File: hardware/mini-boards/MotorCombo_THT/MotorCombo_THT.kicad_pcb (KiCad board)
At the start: 2 copper layers, 75 x 55 mm, 30 parts

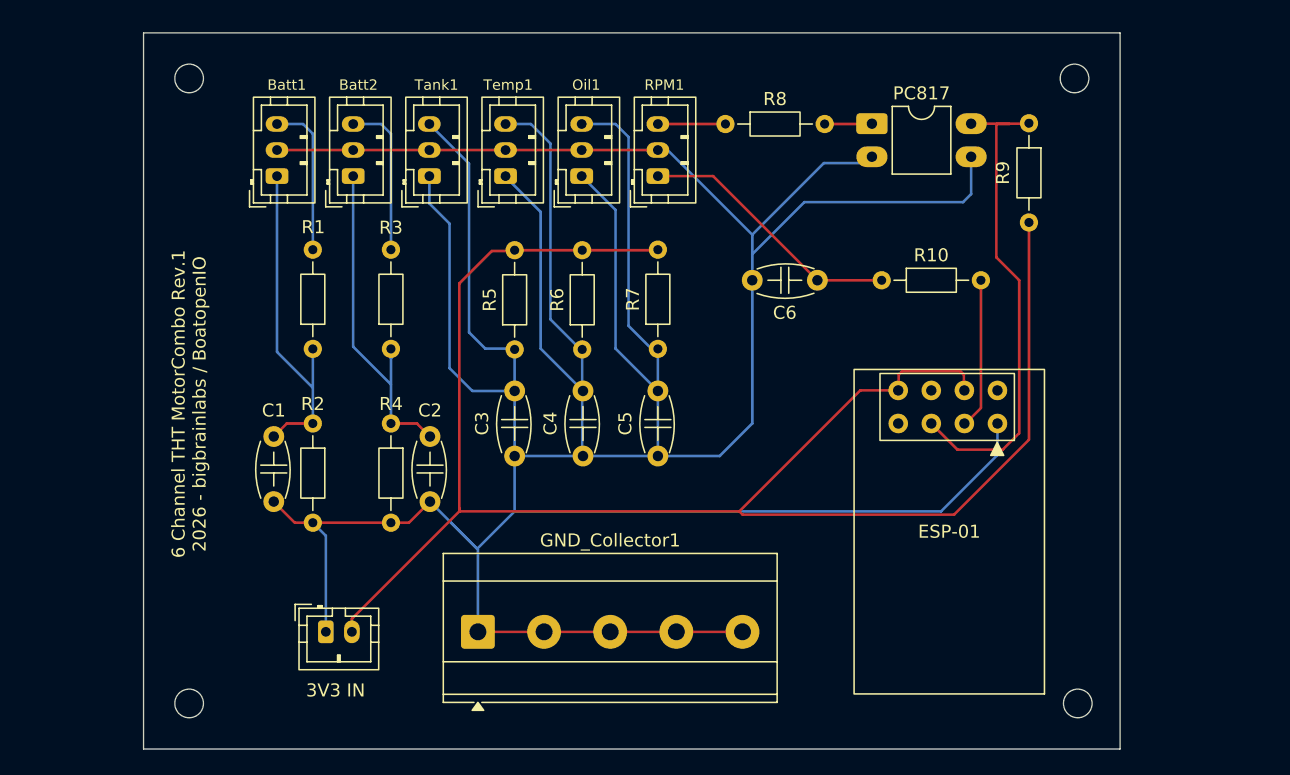
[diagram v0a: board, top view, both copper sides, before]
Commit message: MotorCombo THT: Jumper-Doku, Rev.1-Bild, ESP-01-Firmware; SMD-Variante entfernt
- README (DE/EN): neuer Abschnitt "Kanalmodus — Jumper (Kanäle 1–5)":
  JP1 (P1=3.3V/Pullup, P3=SIG-IN/Teiler, P2=gemeinsam), JP2 und R2 wählen
  Pull-up- vs. Spannungsteiler-Modus je Kanal. Hinweis unter der Kanaltabelle.
- Neues Platinenbild MotorCombo_THT.jpg (Rev.1-Render) eingebunden.
- esp_firmware/esp_firmware.ino wiederhergestellt (ESP-01 Drehzahl: GPIO0
  Impulszählung vom Optokoppler, GPIO2 PWM zum MUX).
- KiCad-Projekt aktualisiert; alte Gerber entfernt.
- MotorCombo/ (SMD-Variante) entfernt.

Co-Authored-By: Claude Opus 4.8 <noreply@anthropic.com>
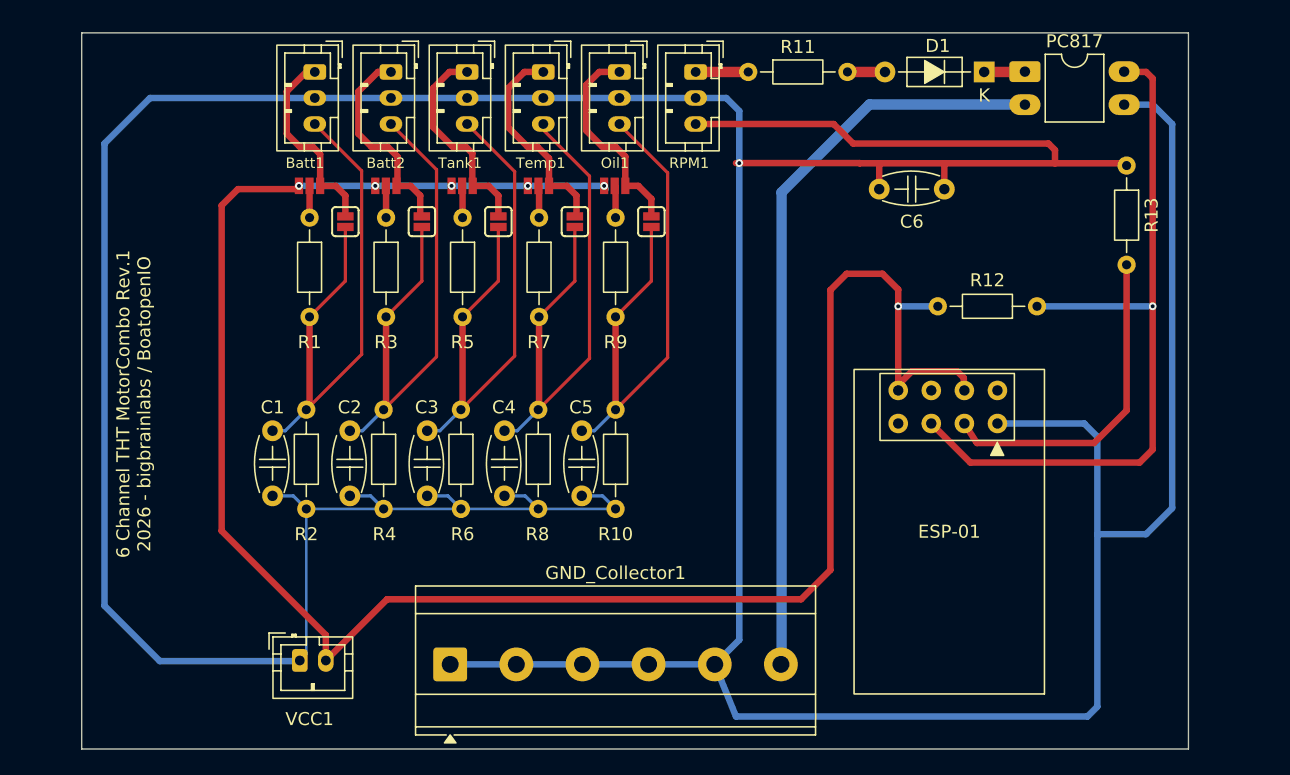
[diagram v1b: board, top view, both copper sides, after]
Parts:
- removed REF** (x4): MountingHole_2.2mm_M2, MountingHole:MountingHole_2.2mm_M2
- added D1: 1N4148, PCM_Diode_THT_AKL:D_DO-35_SOD27_P7.62mm_Horizontal, F.Cu at (118.6, 71.0)
- added JP1: Jumper_3_Open, PCM_SparkFun-Jumper:Jumper_3_NO_NoSilk, F.Cu at (66.8, 79.8)
- added JP10: Jumper_2_Open, PCM_SparkFun-Jumper:Jumper_2_NO, F.Cu at (93.0, 82.5)
- added JP2: Jumper_2_Open, PCM_SparkFun-Jumper:Jumper_2_NO, F.Cu at (69.5, 82.5)
- added JP3: Jumper_3_Open, PCM_SparkFun-Jumper:Jumper_3_NO_NoSilk, F.Cu at (72.6, 79.8)
- added JP4: Jumper_2_Open, PCM_SparkFun-Jumper:Jumper_2_NO, F.Cu at (75.4, 82.5)
- added JP5: Jumper_3_Open, PCM_SparkFun-Jumper:Jumper_3_NO_NoSilk, F.Cu at (78.5, 79.8)
- added JP6: Jumper_2_Open, PCM_SparkFun-Jumper:Jumper_2_NO, F.Cu at (81.2, 82.5)
- added JP7: Jumper_3_Open, PCM_SparkFun-Jumper:Jumper_3_NO_NoSilk, F.Cu at (84.3, 79.8)
- added JP8: Jumper_2_Open, PCM_SparkFun-Jumper:Jumper_2_NO, F.Cu at (87.1, 82.5)
- added JP9: Jumper_3_Open, PCM_SparkFun-Jumper:Jumper_3_NO_NoSilk, F.Cu at (90.2, 79.8)
- added R10: R, Resistor_THT:R_Axial_DIN0204_L3.6mm_D1.6mm_P7.62mm_Horizontal, F.Cu at (90.2, 96.9)
- added R8: R, Resistor_THT:R_Axial_DIN0204_L3.6mm_D1.6mm_P7.62mm_Horizontal, F.Cu at (84.3, 96.9)
- added R9: R, Resistor_THT:R_Axial_DIN0204_L3.6mm_D1.6mm_P7.62mm_Horizontal, F.Cu at (90.2, 82.2)
- GND_Collector1: footprint TerminalBlock_Phoenix:TerminalBlock_Phoenix_MKDS-3-5-5.08_1x05_P5.08mm_Horizontal -> TerminalBlock_Phoenix:TerminalBlock_Phoenix_MKDS-3-6-5.08_1x06_P5.08mm_Horizontal
- R11: renamed from R8; value R -> 1k
- R12: renamed from R9; value R -> 10k
- R13: renamed from R10; value R -> 10k
- VCC1: renamed from 3V3 IN
- moved R13 20.8 mm to (129.5, 78.2), turned to -90 degrees
- moved R12 14.1 mm to (122.6, 89.0), turned to 180 degrees
- moved R7 13.6 mm to (84.4, 82.2), turned to -90 degrees
- moved PC817 12.4 mm to (121.7, 71.0)
- moved R5 10.9 mm to (78.5, 82.2), turned to -90 degrees
- moved R6 10.4 mm to (78.4, 96.9), turned to -90 degrees
- moved R3 10.1 mm to (72.6, 82.2), turned to -90 degrees
- moved R1 10.1 mm to (66.8, 82.2), turned to -90 degrees
- moved Batt1 8.51 mm to (67.2, 71.0), turned to -90 degrees
- moved Batt2 8.51 mm to (73.0, 71.0), turned to -90 degrees
- moved RPM1 8.51 mm to (96.4, 71.0), turned to -90 degrees
- moved Temp1 8.51 mm to (84.7, 71.0), turned to -90 degrees
- moved Oil1 8.51 mm to (90.5, 71.0), turned to -90 degrees
- moved Tank1 8.51 mm to (78.8, 71.0), turned to -90 degrees
- moved C6 8.46 mm to (110.5, 80.0), turned to 0 degrees
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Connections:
- Batt1 pad 1: Net-(Batt1-Pad1) -> Net-(JP1-B)
- Batt2 pad 1: Net-(Batt2-Pad1) -> Net-(JP3-B)
- C3 pad 2: Net-(C3-Pad2) -> Net-(JP6-A)
- C4 pad 2: Net-(C4-Pad2) -> Net-(JP8-A)
- C5 pad 2: Net-(C5-Pad2) -> Net-(JP10-A)
- C6 pad 1: Net-(C6-Pad1) -> GND
- ESP-01 pad 2: Net-(ESP-01-GPIO2) -> Net-(ESP-01-GPIO0)
- ESP-01 pad 3: Net-(ESP-01-GPIO0) -> unconnected-(ESP-01-UTXD-Pad2)
- ESP-01 pad 4: unconnected-(ESP-01-URXD-Pad8) -> unconnected-(ESP-01-RST-Pad6)
- ESP-01 pad 5: unconnected-(ESP-01-RST-Pad5) -> Net-(ESP-01-GPIO2)
- ESP-01 pad 6: Net-(ESP-01-CH_PD) -> unconnected-(ESP-01-URXD-Pad7)
- ESP-01 pad 7: unconnected-(ESP-01-RST-Pad5) -> Net-(ESP-01-CH_PD)
- ESP-01 pad 8: unconnected-(ESP-01-URXD-Pad8) -> Net-(ESP-01-CH_PD)
- Oil1 pad 1: Net-(C5-Pad2) -> Net-(JP10-B)
- Oil1 pad 3: Net-(C5-Pad2) -> Net-(JP10-A)
- PC817 pad 1: Net-(PC817-Pad1) -> Net-(D1-K)
- PC817 pad 2: GND -> Net-(GND_Collector1-Pin_6)
- R1 pad 1: Net-(Batt1-Pad1) -> Net-(JP1-C)
- R11 pad 2: Net-(PC817-Pad1) -> Net-(D1-A)
- R13 pad 1: Net-(C6-Pad1) -> GND
- R3 pad 1: Net-(Batt2-Pad1) -> Net-(JP3-C)
- R5 pad 1: Net-(ESP-01-CH_PD) -> Net-(JP5-C)
- R5 pad 2: Net-(C3-Pad2) -> Net-(JP6-A)
- R6 pad 1: Net-(ESP-01-CH_PD) -> Net-(JP6-A)
- R6 pad 2: Net-(C4-Pad2) -> GND
- R7 pad 1: Net-(ESP-01-CH_PD) -> Net-(JP7-C)
- R7 pad 2: Net-(C5-Pad2) -> Net-(JP8-A)
- RPM1 pad 3: Net-(C6-Pad1) -> GND
- Tank1 pad 1: Net-(C3-Pad2) -> Net-(JP5-B)
- Tank1 pad 3: Net-(C3-Pad2) -> Net-(JP6-A)
- Temp1 pad 1: Net-(C4-Pad2) -> Net-(JP7-B)
- Temp1 pad 3: Net-(C4-Pad2) -> Net-(JP8-A)
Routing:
- net GND: track 171.5 -> 384.0 mm, vias 0 -> 1
- net Net-(C3-Pad2): track 89.9 -> 0.00 mm
- net Net-(ESP-01-CH_PD): track 74.0 -> 148.6 mm, vias 0 -> 6
- net Net-(GND_Collector1-Pin_6): track 0.00 -> 57.8 mm
- net Net-(JP6-A): track 0.00 -> 43.6 mm
- net Net-(JP10-A): track 0.00 -> 43.6 mm
- net Net-(JP8-A): track 0.00 -> 43.5 mm
- net unconnected-(ESP-01-UTXD-Pad1): track 41.3 -> 0.00 mm
- net Net-(C5-Pad2): track 40.3 -> 0.00 mm
- net Net-(C4-Pad2): track 40.0 -> 0.00 mm
- net unconnected-(ESP-01-URXD-Pad8): track 37.8 -> 0.00 mm
- net unconnected-(ESP-01-UTXD-Pad2): track 0.00 -> 25.8 mm
- net Net-(JP4-A): track 20.9 -> 43.6 mm
- net Net-(JP2-A): track 21.4 -> 43.7 mm
- net Net-(C6-Pad1): track 21.1 -> 0.00 mm
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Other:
- board size 75 x 55 mm -> 85 x 55 mm

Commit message: Hardware: Gerber & KiCad-Projektdateien aktualisiert
MotorCombo_THT und v2/input-board: Gerber, Bohrdateien, ZIP,
Bestueckungs-CSV und KiCad-Projektdateien neu erzeugt.

Co-Authored-By: Claude Opus 4.8 <noreply@anthropic.com>
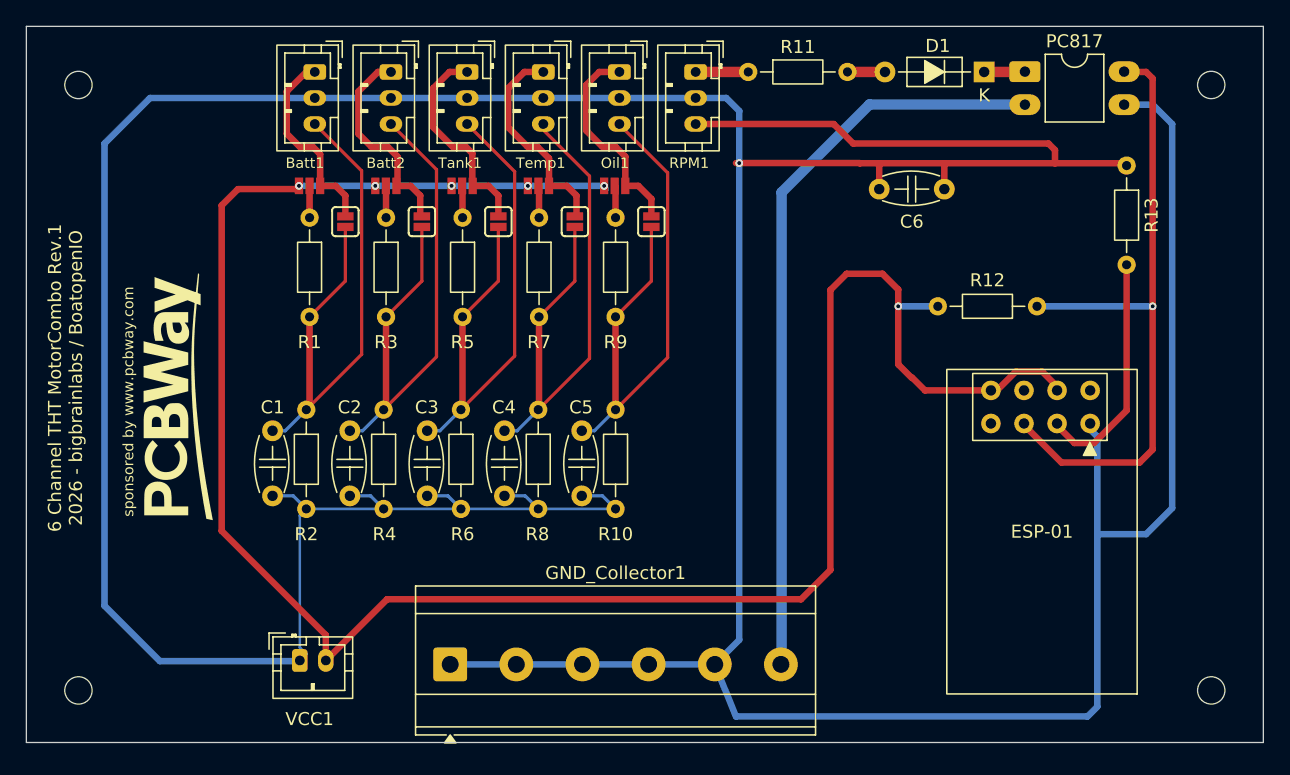
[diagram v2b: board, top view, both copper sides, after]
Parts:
- added REF**: MountingHole_2.1mm, MountingHole:MountingHole_2.1mm, F.Cu at (49.0, 72.0)
- added REF**: MountingHole_2.1mm, MountingHole:MountingHole_2.1mm, F.Cu at (136.0, 72.0)
- added REF**: MountingHole_2.1mm, MountingHole:MountingHole_2.1mm, F.Cu at (136.0, 118.5)
- added REF**: MountingHole_2.1mm, MountingHole:MountingHole_2.1mm, F.Cu at (49.0, 118.5)
- moved ESP-01 7.12 mm to (126.7, 98.0)
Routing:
- net unconnected-(ESP-01-UTXD-Pad2): track 25.8 -> 0.00 mm
- net Net-(ESP-01-GPIO2): track 0.00 -> 18.7 mm
- net Net-(ESP-01-CH_PD): track 148.6 -> 161.0 mm
- net unconnected-(ESP-01-RST-Pad6): track 7.80 -> 0.00 mm
- net Net-(ESP-01-GPIO0): track 58.2 -> 50.7 mm
- net GND: track 384.0 -> 377.6 mm
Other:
- board size 85 x 55 mm -> 95 x 55 mm
- board text added: "sponsored by www.pcbway.com"
